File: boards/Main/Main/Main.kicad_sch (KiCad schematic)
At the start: 29 parts, among them Q1 2N3904, Q2 2N3904, Q3 2N3904

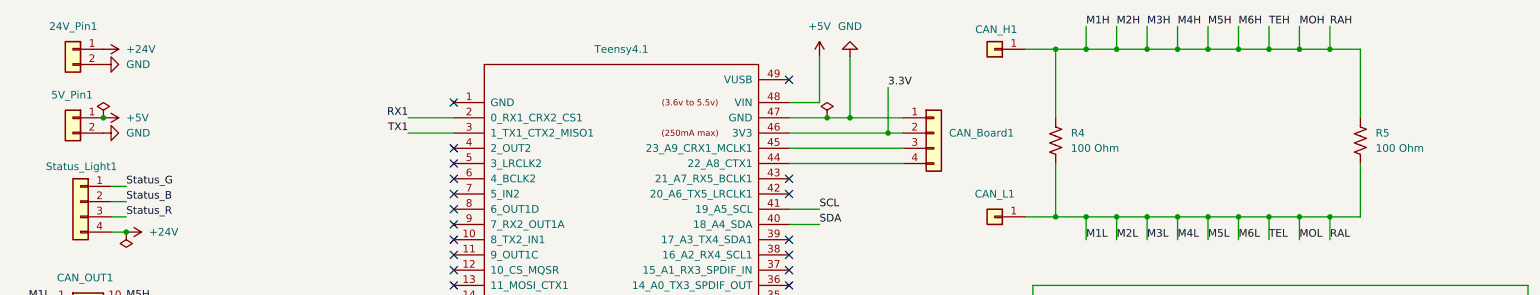
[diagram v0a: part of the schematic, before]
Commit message: Started 4 layer PCB
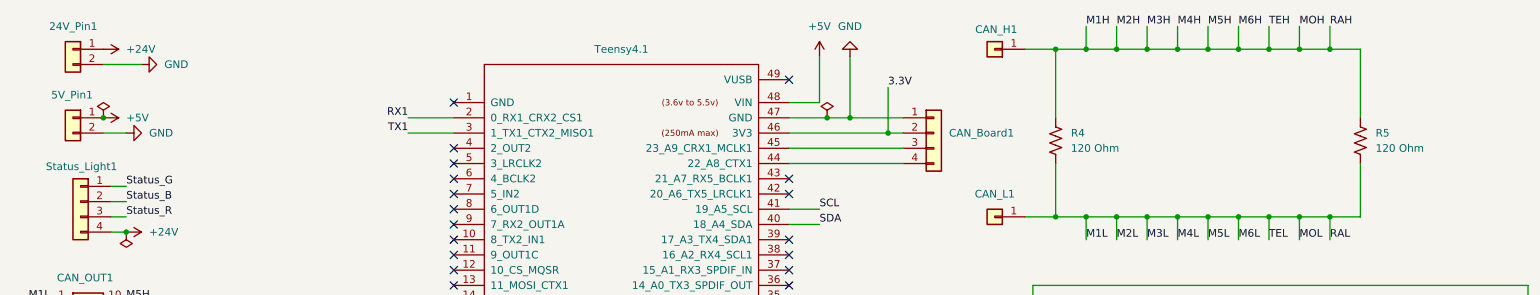
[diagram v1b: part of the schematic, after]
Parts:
- R4, R5: value 100 Ohm -> 120 Ohm
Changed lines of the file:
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@@
 	(wire
 		(pts
+			(xy 33.02 22.86) (xy 26.67 22.86)
+		)
+		(stroke
+			(width 0)
+			(type default)
+		)
+	)
+	(wire
+		(pts
 			(xy 140.97 39.37) (xy 160.02 39.37)
 		)
@@
 	(wire
 		(pts
+			(xy 30.48 34.29) (xy 26.67 34.29)
+		)
+		(stroke
+			(width 0)
+			(type default)
+		)
+	)
+	(wire
+		(pts
 			(xy 163.83 85.09) (xy 165.1 85.09)
 		)
@@
 	(symbol
 		(lib_id "power:GND")
-		(at 26.67 22.86 90)
+		(at 33.02 22.86 90)
 		(unit 1)
 		(exclude_from_sim no)
@@
 		(fields_autoplaced yes)
 		(property "Reference" "#PWR011"
-			(at 33.02 22.86 0)
+			(at 39.37 22.86 0)
 			(effects
 				(font
@@
 		)
 		(property "Value" "GND"
-			(at 30.48 22.8599 90)
+			(at 36.83 22.8599 90)
 			(effects
 				(font
@@
 		)
 		(property "Footprint" ""
-			(at 26.67 22.86 0)
+			(at 33.02 22.86 0)
 			(effects
 				(font
@@
 		)
 		(property "Datasheet" ""
-			(at 26.67 22.86 0)
+			(at 33.02 22.86 0)
 			(effects
 				(font
@@
 		)
 		(property "Description" "Power symbol creates a global label with name \"GND\" , ground"
-			(at 26.67 22.86 0)
+			(at 33.02 22.86 0)
 			(effects
 				(font
@@
 			)
 		)
-		(property "Value" "100 Ohm"
+		(property "Value" "120 Ohm"
 			(at 187.96 36.8299 0)
 			(effects
@@
 			)
 		)
-		(property "Value" "100 Ohm"
+		(property "Value" "120 Ohm"
 			(at 238.76 36.8299 0)
 			(effects
@@
 	(symbol
 		(lib_id "power:GND")
-		(at 26.67 34.29 90)
+		(at 30.48 34.29 90)
 		(unit 1)
 		(exclude_from_sim no)
@@
 		(fields_autoplaced yes)
 		(property "Reference" "#PWR012"
-			(at 33.02 34.29 0)
+			(at 36.83 34.29 0)
 			(effects
 				(font
@@
 		)
 		(property "Value" "GND"
-			(at 30.48 34.2899 90)
+			(at 34.29 34.2899 90)
 			(effects
 				(font
@@
 		)
 		(property "Footprint" ""
-			(at 26.67 34.29 0)
+			(at 30.48 34.29 0)
 			(effects
 				(font
@@
 		)
 		(property "Datasheet" ""
-			(at 26.67 34.29 0)
+			(at 30.48 34.29 0)
 			(effects
 				(font
@@
 		)
 		(property "Description" "Power symbol creates a global label with name \"GND\" , ground"
-			(at 26.67 34.29 0)
+			(at 30.48 34.29 0)
 			(effects
 				(font
